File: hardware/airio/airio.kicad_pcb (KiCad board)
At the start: 2 copper layers, 54 x 24 mm, 25 parts, among them J1 LiPo 1S, J2 GPS, J3 SCREEN, J4 I2C, SW1 TS-1187A-B-A-B, U1 XIAO nRF52840, U2 BMP581, U3 LSM6DSV16X, U4 TCA9534PWR

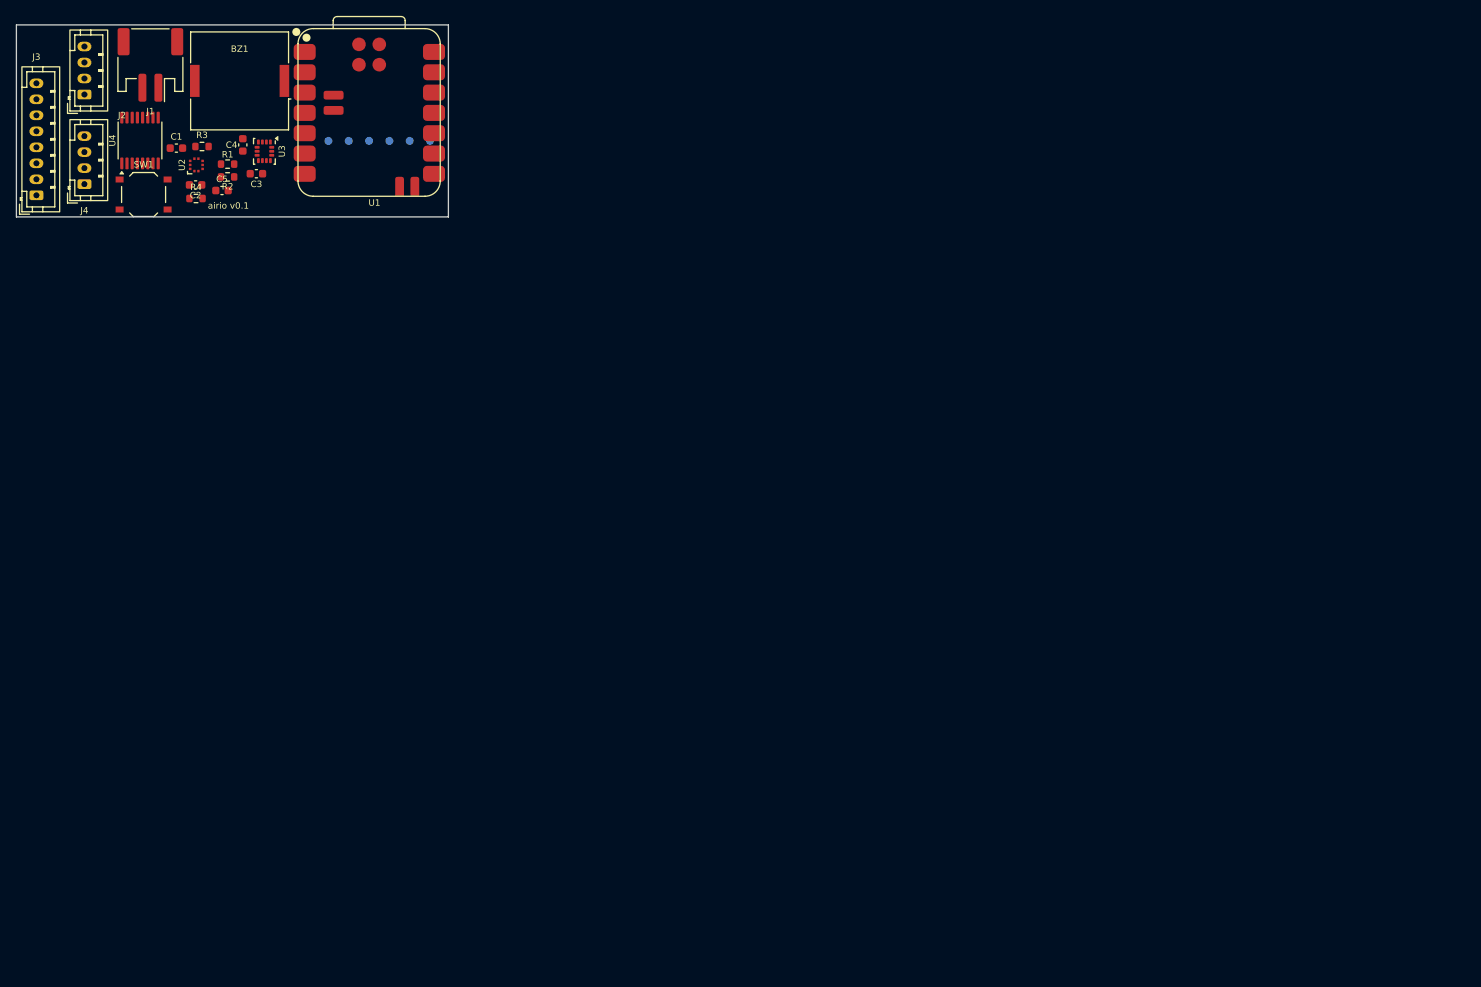
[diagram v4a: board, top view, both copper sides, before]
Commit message: airio: JST SH ports, off-board buzzer, new pin assignment
- J2/J4 SM04B-SRSS-TB and J3 SM08B-SRSS-TB (JST SH, side-entry SMD) replace
  the PH through-hole headers; J1 battery stays JST PH.
- J5 SM02B-SRSS-TB buzzer port replaces the onboard piezo BZ1.
- Max's pin reassignment for easier routing: SPI on D0-D2, I2C on D3/D4,
  EXP_INT on D5, GPS UART on D7/D8, buzzer on D9/D10; D6 spare.
- IMU_INT1 moves to expander P3; SCR_CLK label renamed SCR_SCK so the
  screen clock reaches J3.
- Includes Max's hand placement and routing in progress.
- ERC 0 errors; DRC with schematic parity has no footprint errors.

Co-Authored-By: Claude Opus 5.5 (1M context) <noreply@anthropic.com>
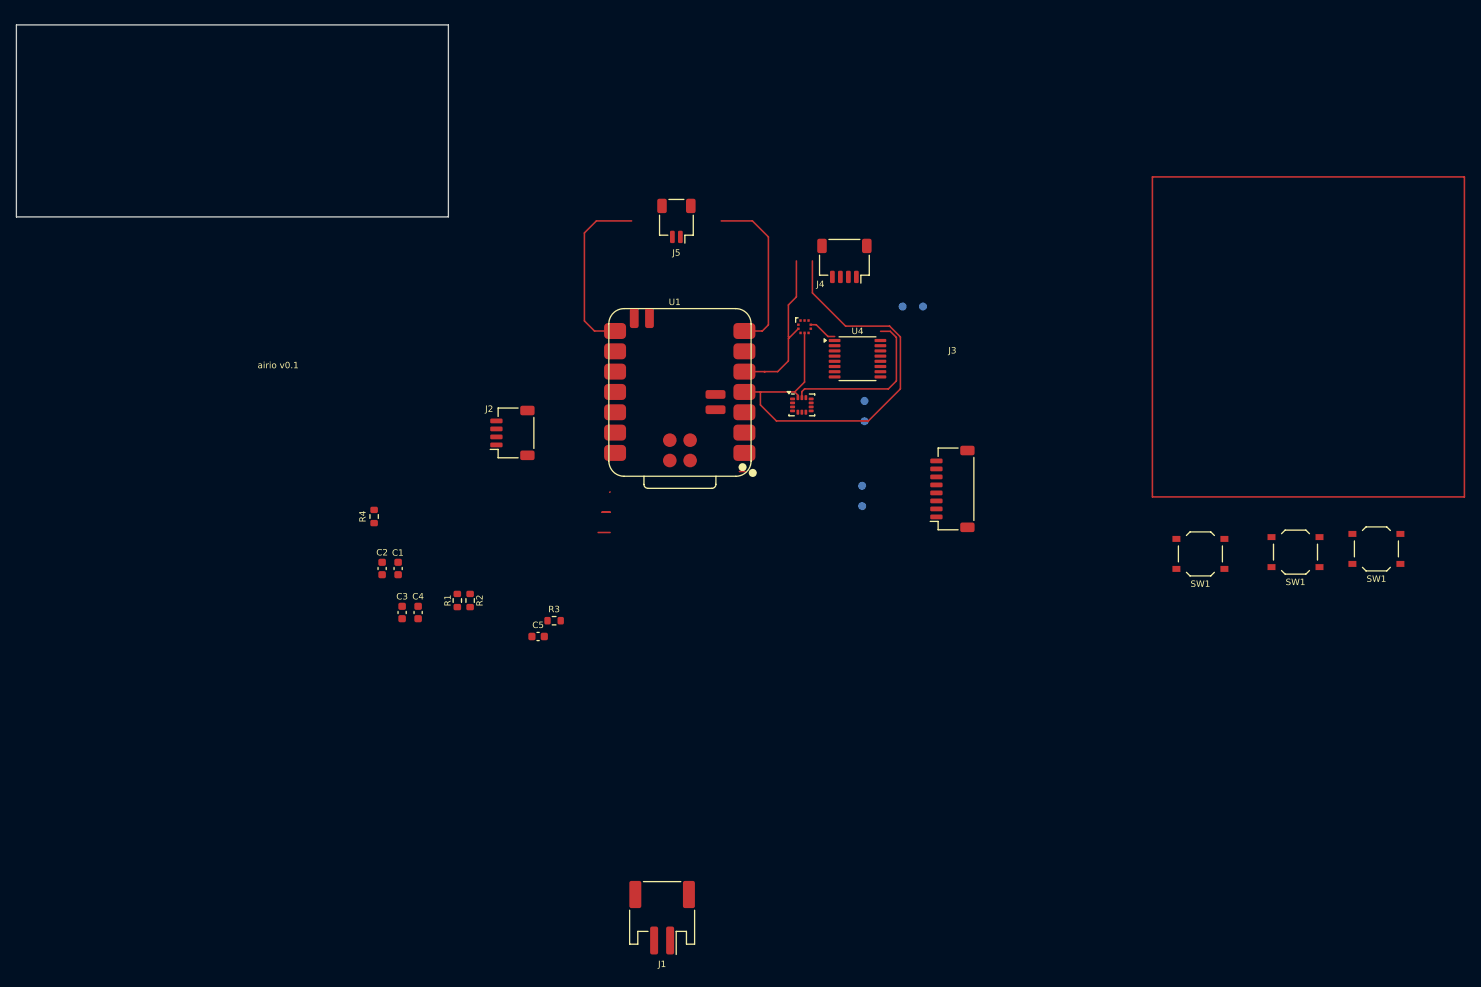
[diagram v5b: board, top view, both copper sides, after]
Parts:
- removed BZ1: PKLCS1212E4001, Buzzer_Beeper:Buzzer_Murata_PKLCS1212E
- added J5: Buzzer, Connector_JST:JST_SH_SM02B-SRSS-TB_1x02-1MP_P1.00mm_Horizontal, F.Cu at (82.5, 24.5)
- added SW1: TS-1187A-B-A-B, Button_Switch_SMD:SW_Push_1P1T_XKB_TS-1187A, F.Cu at (159.9, 65.9)
- added SW1: TS-1187A-B-A-B, Button_Switch_SMD:SW_Push_1P1T_XKB_TS-1187A, F.Cu at (170.0, 65.5)
- J2, J4: footprint Connector_JST:JST_PH_B4B-PH-K_1x04_P2.00mm_Vertical -> Connector_JST:JST_SH_SM04B-SRSS-TB_1x04-1MP_P1.00mm_Horizontal
- J3: footprint Connector_JST:JST_PH_B8B-PH-K_1x08_P2.00mm_Vertical -> Connector_JST:JST_SH_SM08B-SRSS-TB_1x08-1MP_P1.00mm_Horizontal
- moved SW1 139.5 mm to (148.0, 66.1), turned to 180 degrees
- moved J1 124.3 mm to (80.7, 111.6)
- moved J3 120.2 mm to (117.0, 58.0)
- moved J4 95.5 mm to (103.5, 29.5), turned to 180 degrees
- moved U4 93.7 mm to (105.1, 41.7), turned to 0 degrees
- moved U2 78.7 mm to (98.5, 37.7), turned to 0 degrees
- moved TP6 74.5 mm to (106.0, 47.0), turned to -90 degrees
- moved U3 74.3 mm to (98.2, 47.5), turned to 0 degrees
- moved R3 73.8 mm to (67.2, 74.5)
- moved TP5 73.4 mm to (106.0, 49.5), turned to -90 degrees
- moved TP3 71.1 mm to (105.7, 57.6), turned to -90 degrees
- moved TP4 70.7 mm to (105.7, 60.1), turned to -90 degrees
- moved TP2 69.8 mm to (113.3, 35.2)
- moved TP1 69.8 mm to (110.8, 35.2)
- moved C5 68.3 mm to (65.2, 76.4)
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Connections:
- U1 pad 1: /IMU_INT1 -> /SCR_MOSI
- U1 pad 10: /SCR_CS -> /BUZZ_B
- U1 pad 11: /SCR_MOSI -> /BUZZ_A
- U1 pad 2: /GPS_RX -> /SCR_SCK
- U1 pad 3: /BUZZ_A -> /SCR_CS
- U1 pad 4: /BUZZ_B -> /I2C_SDA
- U1 pad 5: /I2C_SDA -> /I2C_SCL
- U1 pad 6: /I2C_SCL -> /EXP_INT
- U1 pad 7: /EXP_INT -> unconnected-(U1-D6-Pad7)
- U1 pad 8: /GPS_TX -> /GPS_RX
- U1 pad 9: /SCR_SCK -> /GPS_TX
- U4 pad 7: unconnected-(U4-P3-Pad7) -> /IMU_INT1
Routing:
- net /I2C_SDA: track 0.00 -> 60.4 mm
- net /I2C_SCL: track 0.00 -> 41.7 mm
- net /GPS_RX: track 0.00 -> 22.6 mm
- net unconnected-(U1-D6-Pad7): track 0.00 -> 21.0 mm
- net /BARO_INT: track 0.00 -> 3.61 mm
- net /EXP_INT: track 0.00 -> 2.00 mm
- net /SCR_MOSI: track 0.00 -> 1.50 mm

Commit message: airio: 3D model for J1 (JST S2B-PH-SM4-TB)
J1 now points to ${KIPRJMOD}/3d/S2B-PH-SM4-TB.STEP, aligned to the
footprint (rotate -90 X, offset -7.9, 12.7, 0). JST's STEP file is not
committed; the README says where to download it. Includes Max's latest
layout edits.

Co-Authored-By: Claude Opus 5.5 (1M context) <noreply@anthropic.com>
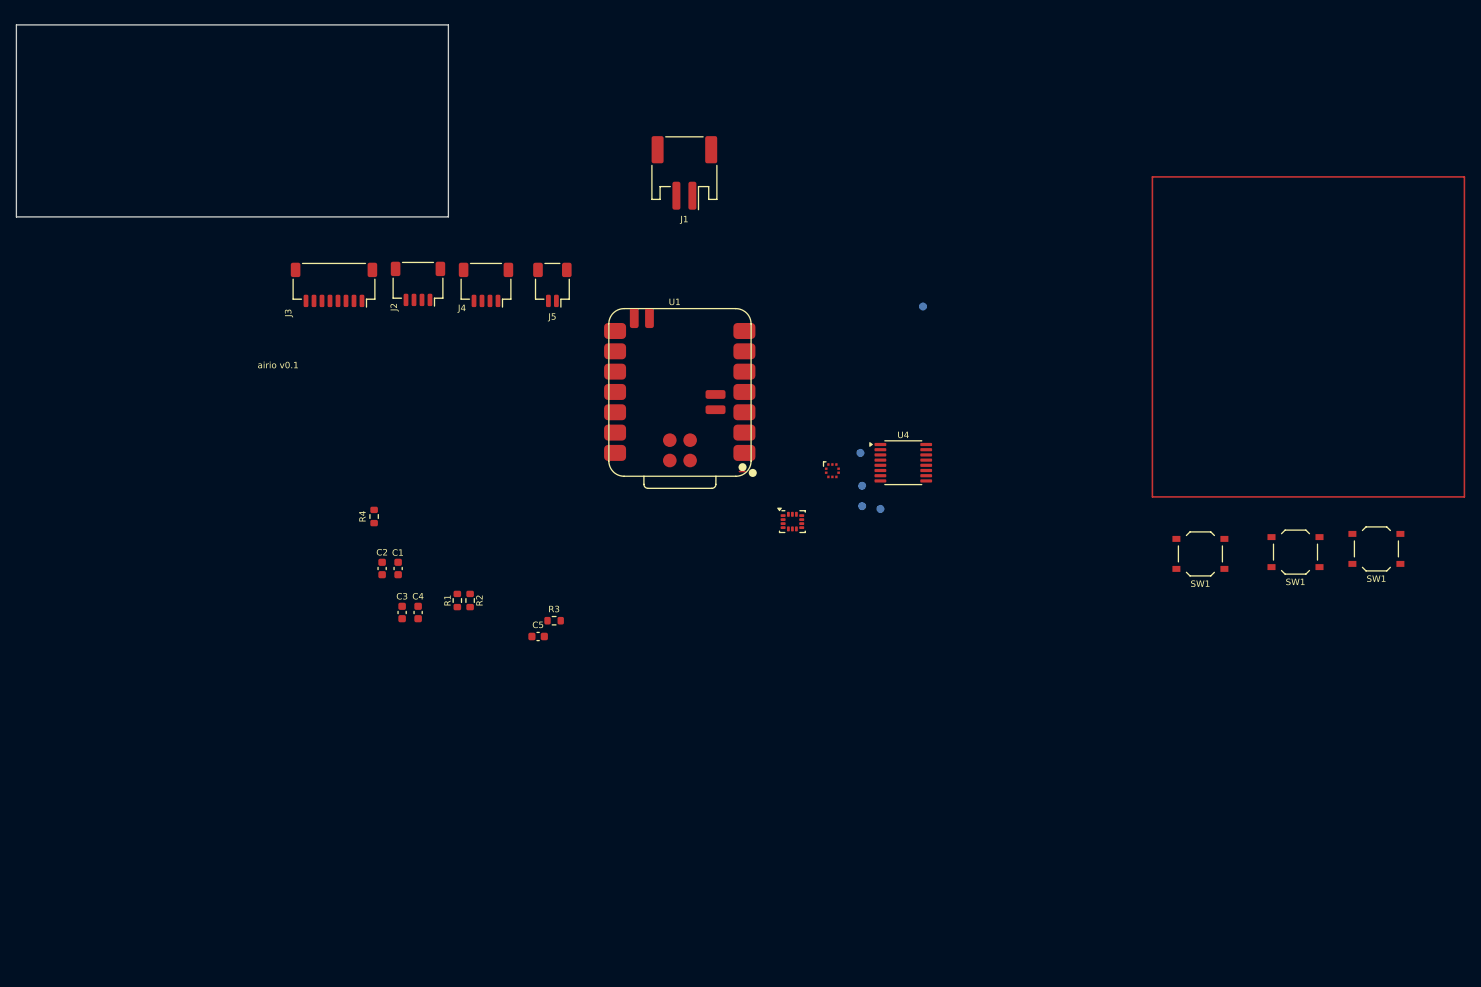
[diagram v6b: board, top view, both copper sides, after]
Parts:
- removed TP1: SWDIO, TestPoint:TestPoint_Pad_D1.0mm
- moved J1 93.1 mm to (83.5, 18.5)
- moved J3 81.4 mm to (39.7, 32.5), turned to 180 degrees
- moved J4 44.9 mm to (58.7, 32.5)
- moved J2 22.0 mm to (50.2, 32.4), turned to 180 degrees
- moved U2 18.3 mm to (102.0, 55.7)
- moved J5 17.4 mm to (67.0, 32.5)
- moved U3 14.6 mm to (97.0, 62.1)
- moved U4 14.2 mm to (110.9, 54.7)
- moved TP6 13.6 mm to (108.0, 60.5)
- moved TP5 3.99 mm to (105.5, 53.5)
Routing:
- net /I2C_SDA: track 60.4 -> 0.00 mm
- net /I2C_SCL: track 41.7 -> 0.00 mm
- net /GPS_RX: track 22.6 -> 0.72 mm
- net unconnected-(U1-D6-Pad7): track 21.0 -> 0.00 mm
- net /BARO_INT: track 3.61 -> 0.00 mm
- net /EXP_INT: track 2.00 -> 0.00 mm
- net /SCR_MOSI: track 1.50 -> 0.00 mm

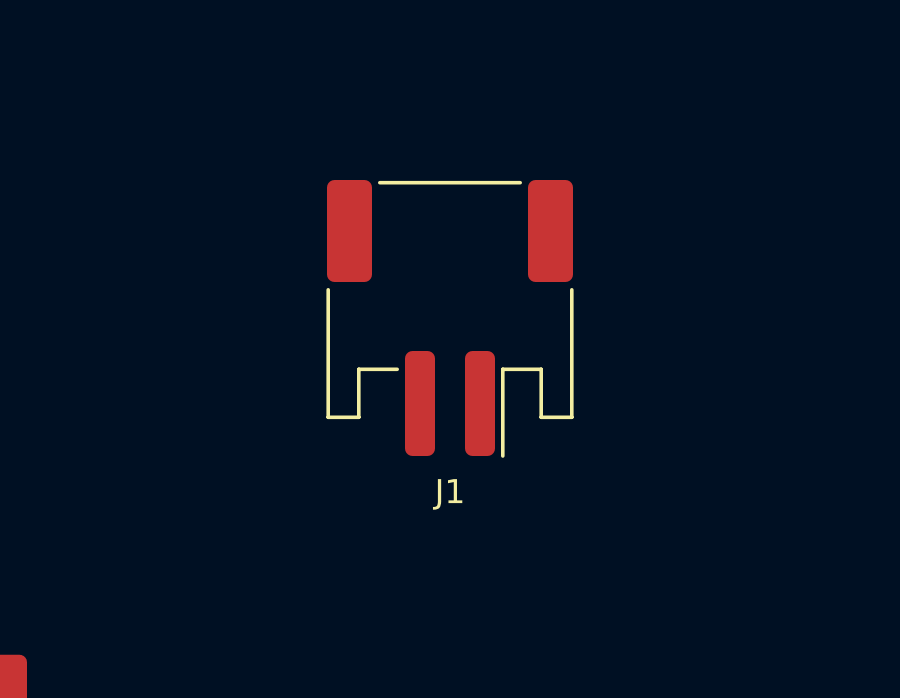
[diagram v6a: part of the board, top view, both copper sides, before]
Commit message: airio: J1 to through-hole PH on the back; restore SH ports
- J1 is now JST S2B-PH-K-S (THT, side entry), flipped to the bottom side.
- Max's latest pin assignment: buzzer on D6/D7, GPS on D9/D10 (J2 pin 3
  GPS RX, pin 4 GPS TX), screen on D0-D2 with J3 reordered, BARO_INT on
  U4 P0, IMU_INT1 on P1, SCR_DISP on P2; D8 spare.
- A schematic save from an older editor session had undone the SH change;
  J2/J4 SM04B, J3 SM08B and J5 SM02B (replacing BZ1) are re-applied.
- BTN had lost its expander pin; it is now on U4 P3.
- ERC 0 errors; DRC parity: no footprint mismatches (TP1 missing on the
  board, two duplicate SW1 footprints).

Co-Authored-By: Claude Opus 5.5 (1M context) <noreply@anthropic.com>
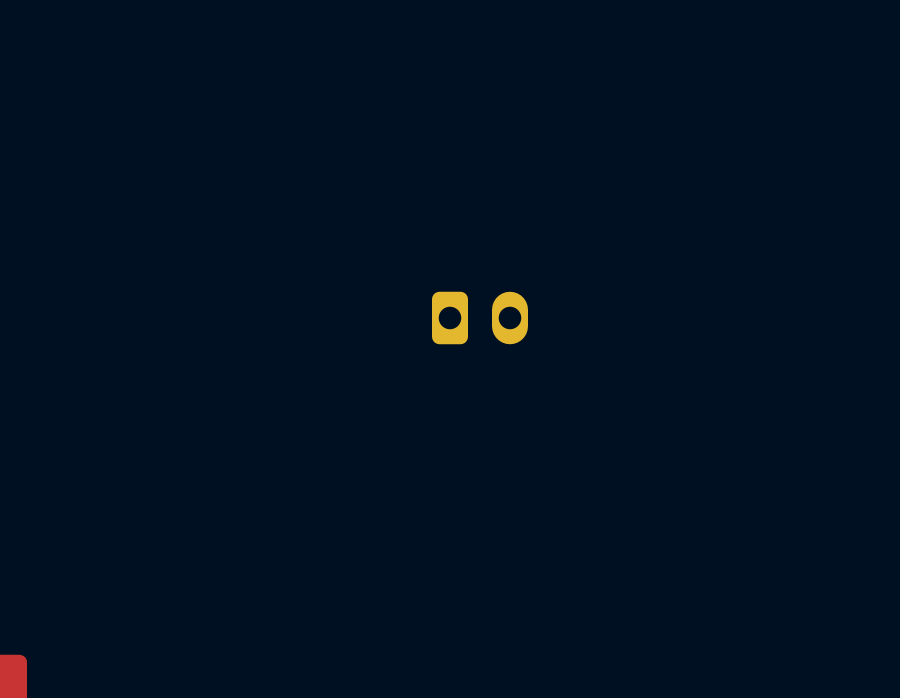
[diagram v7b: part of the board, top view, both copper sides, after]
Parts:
- J1: footprint Connector_JST:JST_PH_S2B-PH-SM4-TB_1x02-1MP_P2.00mm_Horizontal -> Connector_JST:JST_PH_S2B-PH-K_1x02_P2.00mm_Horizontal; moved to B.Cu
- turned J1 to 0 degrees
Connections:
- J2 pad 3: /GPS_TX -> /GPS_RX
- J2 pad 4: /GPS_RX -> /GPS_TX
- J3 pad 4: /SCR_SCK -> /SCR_DISP
- J3 pad 5: /SCR_MOSI -> /SCR_CS
- J3 pad 6: /SCR_CS -> /SCR_CLK
- J3 pad 7: /SCR_DISP -> /SCR_MOSI
- U1 pad 10: /BUZZ_B -> /GPS_TX
- U1 pad 11: /BUZZ_A -> /GPS_RX
- U1 pad 2: /SCR_SCK -> /SCR_CLK
- U1 pad 7: unconnected-(U1-D6-Pad7) -> /BUZZ_A
- U1 pad 8: /GPS_RX -> /BUZZ_B
- U1 pad 9: /GPS_TX -> unconnected-(U1-D8-Pad9)
- U4 pad 4: /BTN -> /BARO_INT
- U4 pad 5: /BARO_INT -> /IMU_INT1
- U4 pad 7: /IMU_INT1 -> /BTN
